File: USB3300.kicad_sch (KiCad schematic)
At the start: 48 parts, among them J1 SWD, J3 USB_C_Receptacle_USB2.0_14P, SW1 SW_SPDT, U1 USB3300-EZK, U2 STM32F405RGT6, U3 XC6206PxxxMR, U4 SRV05-4, Y1 16MHz, Y2 24MHz

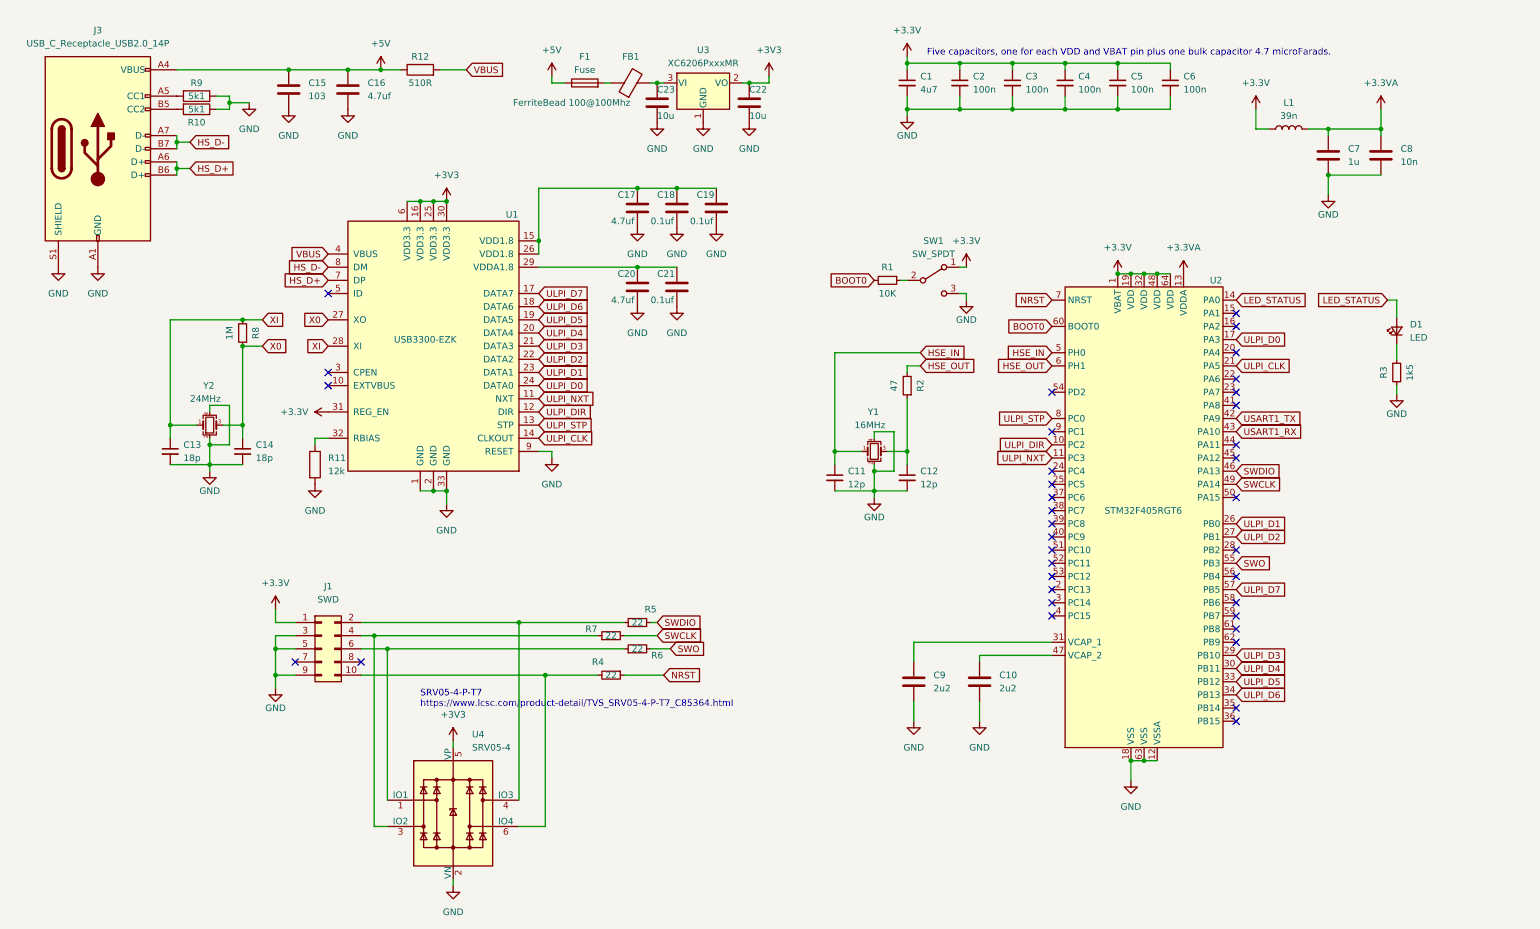
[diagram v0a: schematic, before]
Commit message: Added power_flags to lower the amount of warnings, fixed +3V3 label
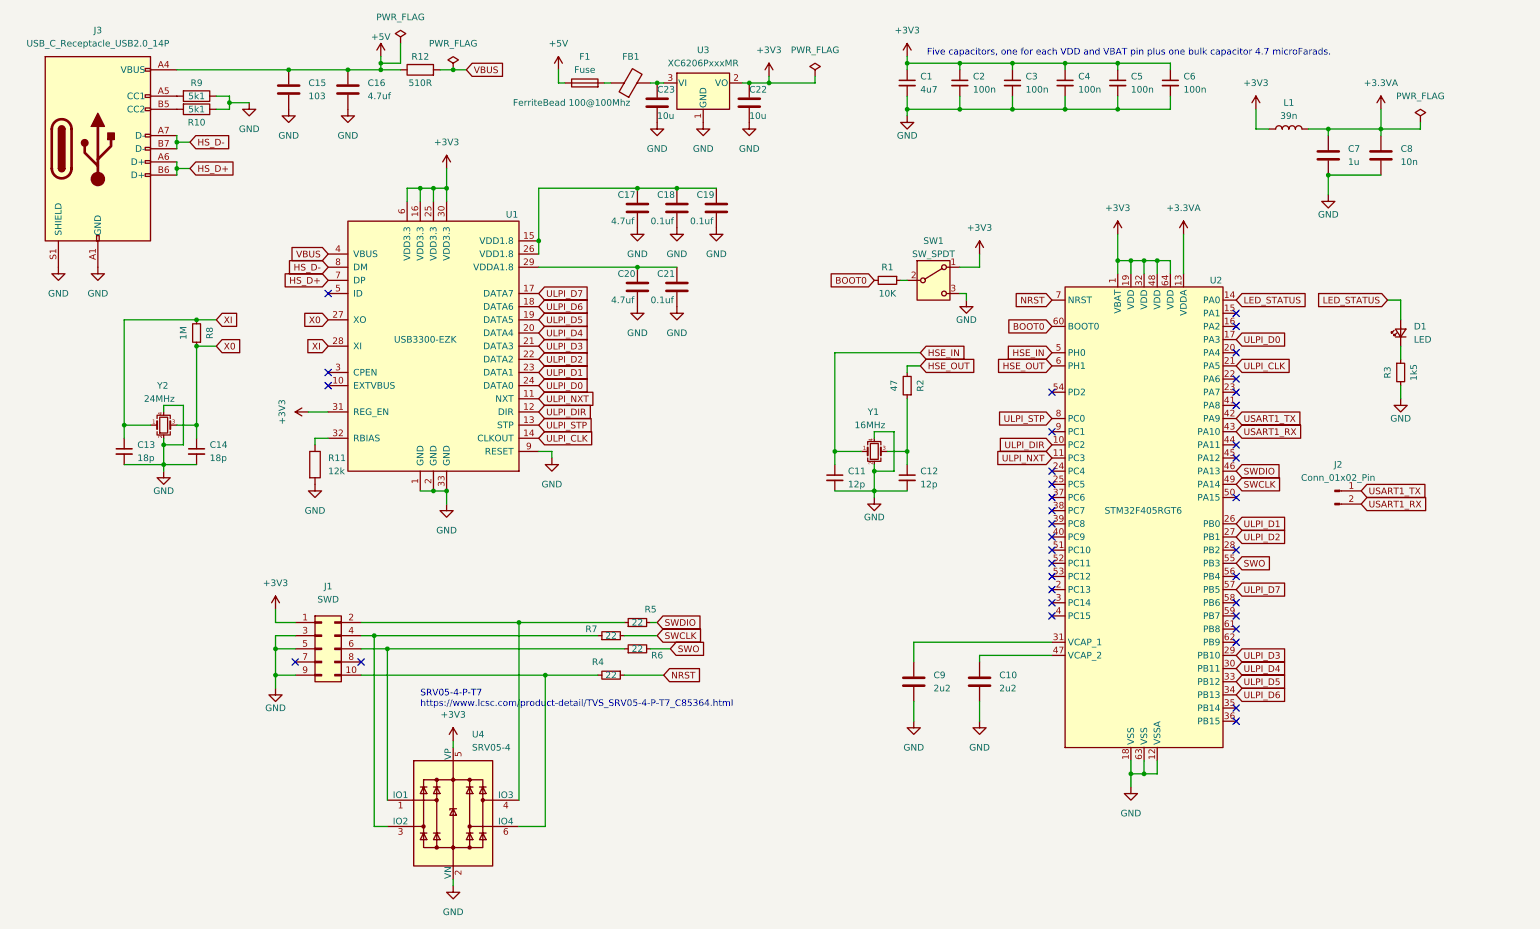
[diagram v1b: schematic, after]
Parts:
- added J2: Conn_01x02_Pin, symbol Connector:Conn_01x02_Pin
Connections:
- net +3.3V is gone; now on net +3V3: L1.1, U1.31 (REG_EN), U2.1 (VBAT), U2.19 (VDD), U2.32 (VDD), U2.48 (VDD), U2.64 (VDD)
- net USART1_RX: now also J2.2 (Pin_2)
- net USART1_TX: now also J2.1 (Pin_1)
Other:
- moved on the sheet: C13, C14, D1, R3, R8, Y2

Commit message: layout
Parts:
- C10, C15, C16, C17, C18, C19, C20, C21, C22, C23, C7, C8, C9: footprint (none) -> Capacitor_SMD:C_0603_1608Metric
- C13, C14, C2, C3, C4, C5, C6: footprint Capacitor_SMD:C_0402_1005Metric -> Capacitor_SMD:C_0603_1608Metric
- F1: footprint (none) -> Fuse:Fuse_1206_3216Metric_Pad1.42x1.75mm_HandSolder
- FB1: footprint (none) -> Ferrite_THT:LairdTech_28C0236-0JW-10
- J2: footprint (none) -> Connector_PinHeader_2.54mm:PinHeader_1x02_P2.54mm_Vertical
- J3: footprint (none) -> Connector_USB:USB_Micro-B_Molex-105017-0001
- L1: footprint (none) -> Inductor_SMD:L_0603_1608Metric
- R10, R11, R12, R9: footprint (none) -> Resistor_SMD:R_0603_1608Metric
- R2, R4, R5, R6, R7, R8: footprint Resistor_SMD:R_0402_1005Metric -> Resistor_SMD:R_0603_1608Metric
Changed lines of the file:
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@@
       (effects (font (size 1.27 1.27)) (justify left))
     )
-    (property "Footprint" "" (at 65.7352 29.21 0)
+    (property "Footprint" "Capacitor_SMD:C_0603_1608Metric" (at 65.7352 29.21 0)
       (effects (font (size 1.27 1.27)) hide)
     )
@@
       (effects (font (size 1.27 1.27)) (justify left))
     )
-    (property "Footprint" "Capacitor_SMD:C_0402_1005Metric" (at 194.31 24.13 0)
+    (property "Footprint" "Capacitor_SMD:C_0603_1608Metric" (at 194.31 24.13 0)
       (effects (font (size 1.27 1.27)) hide)
     )
@@
       (effects (font (size 1.27 1.27)))
     )
-    (property "Footprint" "" (at 46.99 27.432 90)
+    (property "Footprint" "Resistor_SMD:R_0603_1608Metric" (at 46.99 27.432 90)
       (effects (font (size 1.27 1.27)) hide)
     )
@@
       (effects (font (size 1.27 1.27)))
     )
-    (property "Footprint" "Resistor_SMD:R_0402_1005Metric" (at 132.08 128.27 0)
+    (property "Footprint" "Resistor_SMD:R_0603_1608Metric" (at 132.08 128.27 0)
       (effects (font (size 1.27 1.27)) hide)
     )
@@
       (effects (font (size 1.27 1.27)))
     )
-    (property "Footprint" "Resistor_SMD:R_0402_1005Metric" (at 184.15 82.55 0)
+    (property "Footprint" "Resistor_SMD:R_0603_1608Metric" (at 184.15 82.55 0)
       (effects (font (size 1.27 1.27)) hide)
     )
@@
       (effects (font (size 1.27 1.27)) (justify left))
     )
-    (property "Footprint" "Capacitor_SMD:C_0402_1005Metric" (at 224.79 24.13 0)
+    (property "Footprint" "Capacitor_SMD:C_0603_1608Metric" (at 224.79 24.13 0)
       (effects (font (size 1.27 1.27)) hide)
     )
@@
       (effects (font (size 1.27 1.27)) (justify left))
     )
-    (property "Footprint" "Capacitor_SMD:C_0402_1005Metric" (at 234.95 24.13 0)
+    (property "Footprint" "Capacitor_SMD:C_0603_1608Metric" (at 234.95 24.13 0)
       (effects (font (size 1.27 1.27)) hide)
     )
@@
       (effects (font (size 1.27 1.27)))
     )
-    (property "Footprint" "" (at 121.92 25.908 90)
+    (property "Footprint" "Fuse:Fuse_1206_3216Metric_Pad1.42x1.75mm_HandSolder" (at 121.92 25.908 90)
       (effects (font (size 1.27 1.27)) hide)
     )
@@
       (effects (font (size 1.27 1.27)) (justify left))
     )
-    (property "Footprint" "" (at 276.5552 41.91 0)
+    (property "Footprint" "Capacitor_SMD:C_0603_1608Metric" (at 276.5552 41.91 0)
       (effects (font (size 1.27 1.27)) hide)
     )
@@
       (effects (font (size 1.27 1.27)) (justify left))
     )
-    (property "Footprint" "" (at 77.1652 29.21 0)
+    (property "Footprint" "Capacitor_SMD:C_0603_1608Metric" (at 77.1652 29.21 0)
       (effects (font (size 1.27 1.27)) hide)
     )
@@
       (effects (font (size 1.27 1.27)))
     )
-    (property "Footprint" "" (at 31.75 36.83 0)
+    (property "Footprint" "Connector_USB:USB_Micro-B_Molex-105017-0001" (at 31.75 36.83 0)
       (effects (font (size 1.27 1.27)) hide)
     )
@@
       (effects (font (size 1.27 1.27)))
     )
-    (property "Footprint" "Resistor_SMD:R_0402_1005Metric" (at 127 138.43 0)
+    (property "Footprint" "Resistor_SMD:R_0603_1608Metric" (at 127 138.43 0)
       (effects (font (size 1.27 1.27)) hide)
     )
@@
       (effects (font (size 1.27 1.27)) (justify left))
     )
-    (property "Footprint" "" (at 186.3852 143.51 0)
+    (property "Footprint" "Capacitor_SMD:C_0603_1608Metric" (at 186.3852 143.51 0)
       (effects (font (size 1.27 1.27)) hide)
     )
@@
       (effects (font (size 1.27 1.27)))
     )
-    (property "Footprint" "" (at 130.81 25.908 90)
+    (property "Footprint" "Ferrite_THT:LairdTech_28C0236-0JW-10" (at 130.81 25.908 90)
       (effects (font (size 1.27 1.27)) hide)
     )
@@
       (effects (font (size 1.27 1.27)))
     )
-    (property "Footprint" "" (at 257.81 33.02 0)
+    (property "Footprint" "Inductor_SMD:L_0603_1608Metric" (at 257.81 33.02 0)
       (effects (font (size 1.27 1.27)) hide)
     )
@@
       (effects (font (size 1.27 1.27)))
     )
-    (property "Footprint" "" (at 46.99 24.892 90)
+    (property "Footprint" "Resistor_SMD:R_0603_1608Metric" (at 46.99 24.892 90)
       (effects (font (size 1.27 1.27)) hide)
     )
@@
       (effects (font (size 1.27 1.27)) (justify left))
     )
-    (property "Footprint" "Capacitor_SMD:C_0402_1005Metric" (at 46.99 95.25 0)
+    (property "Footprint" "Capacitor_SMD:C_0603_1608Metric" (at 46.99 95.25 0)
       (effects (font (size 1.27 1.27)) hide)
     )
@@
       (effects (font (size 1.27 1.27)) (justify left))
     )
-    (property "Footprint" "" (at 154.6352 31.75 0)
+    (property "Footprint" "Capacitor_SMD:C_0603_1608Metric" (at 154.6352 31.75 0)
       (effects (font (size 1.27 1.27)) hide)
     )
@@
       (effects (font (size 1.27 1.27)) (justify left))
     )
-    (property "Footprint" "" (at 133.0452 52.07 0)
+    (property "Footprint" "Capacitor_SMD:C_0603_1608Metric" (at 133.0452 52.07 0)
       (effects (font (size 1.27 1.27)) hide)
     )
@@
       (effects (font (size 1.27 1.27)))
     )
-    (property "Footprint" "Resistor_SMD:R_0402_1005Metric" (at 127 130.81 0)
+    (property "Footprint" "Resistor_SMD:R_0603_1608Metric" (at 127 130.81 0)
       (effects (font (size 1.27 1.27)) hide)
     )
@@
       (effects (font (size 1.27 1.27)) (justify left))
     )
-    (property "Footprint" "" (at 148.2852 52.07 0)
+    (property "Footprint" "Capacitor_SMD:C_0603_1608Metric" (at 148.2852 52.07 0)
       (effects (font (size 1.27 1.27)) hide)
     )
@@
       (effects (font (size 1.27 1.27)))
     )
-    (property "Footprint" "Resistor_SMD:R_0402_1005Metric" (at 132.08 133.35 0)
+    (property "Footprint" "Resistor_SMD:R_0603_1608Metric" (at 132.08 133.35 0)
       (effects (font (size 1.27 1.27)) hide)
     )
@@
       (effects (font (size 1.27 1.27)) (justify left))
     )
-    (property "Footprint" "" (at 266.3952 41.91 0)
+    (property "Footprint" "Capacitor_SMD:C_0603_1608Metric" (at 266.3952 41.91 0)
       (effects (font (size 1.27 1.27)) hide)
     )
@@
       (effects (font (size 1.27 1.27)) (justify left))
     )
-    (property "Footprint" "Capacitor_SMD:C_0402_1005Metric" (at 204.47 24.13 0)
+    (property "Footprint" "Capacitor_SMD:C_0603_1608Metric" (at 204.47 24.13 0)
       (effects (font (size 1.27 1.27)) hide)
     )
@@
       (effects (font (size 1.27 1.27)) (justify left))
     )
-    (property "Footprint" "" (at 136.8552 31.75 0)
+    (property "Footprint" "Capacitor_SMD:C_0603_1608Metric" (at 136.8552 31.75 0)
       (effects (font (size 1.27 1.27)) hide)
     )
@@
       (effects (font (size 1.27 1.27)) (justify left))
     )
-    (property "Footprint" "" (at 133.0452 67.31 0)
+    (property "Footprint" "Capacitor_SMD:C_0603_1608Metric" (at 133.0452 67.31 0)
       (effects (font (size 1.27 1.27)) hide)
     )
@@
       (effects (font (size 1.27 1.27)) (justify left))
     )
-    (property "Footprint" "" (at 199.0852 143.51 0)
+    (property "Footprint" "Capacitor_SMD:C_0603_1608Metric" (at 199.0852 143.51 0)
       (effects (font (size 1.27 1.27)) hide)
     )
@@
       (effects (font (size 1.27 1.27)))
     )
-    (property "Footprint" "" (at 90.17 23.368 90)
+    (property "Footprint" "Resistor_SMD:R_0603_1608Metric" (at 90.17 23.368 90)
       (effects (font (size 1.27 1.27)) hide)
     )
@@
       (effects (font (size 1.27 1.27)) (justify left))
     )
-    (property "Footprint" "" (at 140.6652 52.07 0)
+    (property "Footprint" "Capacitor_SMD:C_0603_1608Metric" (at 140.6652 52.07 0)
       (effects (font (size 1.27 1.27)) hide)
     )
@@
       (effects (font (size 1.27 1.27)) (justify left))
     )
-    (property "Footprint" "Capacitor_SMD:C_0402_1005Metric" (at 214.63 24.13 0)
+    (property "Footprint" "Capacitor_SMD:C_0603_1608Metric" (at 214.63 24.13 0)
       (effects (font (size 1.27 1.27)) hide)
     )
@@
       (effects (font (size 1.27 1.27)))
     )
-    (property "Footprint" "Resistor_SMD:R_0402_1005Metric" (at 46.99 72.39 0)
+    (property "Footprint" "Resistor_SMD:R_0603_1608Metric" (at 46.99 72.39 0)
       (effects (font (size 1.27 1.27)) hide)
     )
@@
       (effects (font (size 1.27 1.27)) (justify left))
     )
-    (property "Footprint" "Capacitor_SMD:C_0402_1005Metric" (at 33.02 95.25 0)
+    (property "Footprint" "Capacitor_SMD:C_0603_1608Metric" (at 33.02 95.25 0)
       (effects (font (size 1.27 1.27)) hide)
     )
@@
       (effects (font (size 1.27 1.27)))
     )
-    (property "Footprint" "" (at 266.7 102.87 0)
+    (property "Footprint" "Connector_PinHeader_2.54mm:PinHeader_1x02_P2.54mm_Vertical" (at 266.7 102.87 0)
       (effects (font (size 1.27 1.27)) hide)
     )
@@
       (effects (font (size 1.27 1.27)) (justify left))
     )
-    (property "Footprint" "" (at 140.6652 67.31 0)
+    (property "Footprint" "Capacitor_SMD:C_0603_1608Metric" (at 140.6652 67.31 0)
       (effects (font (size 1.27 1.27)) hide)
     )
@@
       (effects (font (size 1.27 1.27)) (justify left))
     )
-    (property "Footprint" "" (at 68.072 97.79 90)
-      (effects (font (size 1.27 1.27)) hide)
-    )
+    (property "Footprint" "Resistor_SMD:R_0603_1608Metric" (at 68.072 97.79 90)
+      (effects (font (size 1.27 1.27)) hide)
+    )

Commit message: work on pcb
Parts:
- added C24: 100n, symbol Device:C
- J3: footprint Connector_USB:USB_Micro-B_Molex-105017-0001 -> Connector_USB:USB_C_Receptacle_HRO_TYPE-C-31-M-12
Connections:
- net GND: now also C24.2
- net NRST: now also C24.1
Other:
- note added: "pull up"
- note added: "pull up 10k am uart auf 3V3"
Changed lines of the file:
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@@
   (junction (at 64.77 21.59) (diameter 0) (color 0 0 0 0)
+  )
+  (junction (at 134.62 138.43) (diameter 0) (color 0 0 0 0)
   )
   (junction (at 132.08 59.69) (diameter 0) (color 0 0 0 0)
@@
     (stroke (width 0) (type default))
   )
-  (wire (pts (xy 129.54 138.43) (xy 137.16 138.43))
+  (wire (pts (xy 129.54 138.43) (xy 134.62 138.43))
     (stroke (width 0) (type default))
   )
@@
     (stroke (width 0) (type default))
   )
+  (wire (pts (xy 134.62 138.43) (xy 134.62 151.13))
+    (stroke (width 0) (type default))
+  )
   (wire (pts (xy 184.15 85.09) (xy 184.15 95.25))
     (stroke (width 0) (type solid))
@@
     (stroke (width 0) (type default))
   )
+  (wire (pts (xy 134.62 138.43) (xy 137.16 138.43))
+    (stroke (width 0) (type default))
+  )
   (wire (pts (xy 214.63 29.21) (xy 204.47 29.21))
     (stroke (width 0) (type solid))
@@
   (wire (pts (xy 251.46 29.21) (xy 251.46 33.02))
     (stroke (width 0) (type default))
+  )
+  (text "pull up" (at 59.69 91.44 0)
+    (effects (font (size 1.27 1.27)) (justify left bottom))
   )
   (text "Five capacitors, one for each VDD and VBAT pin plus one bulk capacitor 4.7 microFarads."
     (at 187.96 19.05 0)
+    (effects (font (size 1.27 1.27)) (justify left bottom))
+  )
+  (text "pull up 10k am uart auf 3V3" (at 270.51 110.49 0)
     (effects (font (size 1.27 1.27)) (justify left bottom))
   )
@@
     )
   )
+  (symbol (lib_id "Device:C") (at 134.62 154.94 0) (unit 1)
+    (in_bom yes) (on_board yes) (dnp no) (fields_autoplaced)
+    (property "Reference" "C24" (at 138.43 153.67 0)
+      (effects (font (size 1.27 1.27)) (justify left))
+    )
+    (property "Value" "100n" (at 138.43 156.21 0)
+      (effects (font (size 1.27 1.27)) (justify left))
+    )
+    (property "Footprint" "" (at 135.5852 158.75 0)
+      (effects (font (size 1.27 1.27)) hide)
+    )
+    (property "Datasheet" "~" (at 134.62 154.94 0)
+      (effects (font (size 1.27 1.27)) hide)
+    )
+    (pin "1")
+    (pin "2")
+    (instances
+      (project "USB3300"
+        (path "/09e9d231-c510-4f8a-ac7d-12061987ad81"
+          (reference "C24") (unit 1)
+        )
+      )
+    )
+  )
   (symbol (lib_id "power:GND") (at 62.23 140.97 0) (unit 1)
     (in_bom yes) (on_board yes) (dnp no)
@@
       (effects (font (size 1.27 1.27)))
     )
-    (property "Footprint" "Connector_USB:USB_Micro-B_Molex-105017-0001" (at 31.75 36.83 0)
+    (property "Footprint" "Connector_USB:USB_C_Receptacle_HRO_TYPE-C-31-M-12" (at 31.75 36.83 0)
       (effects (font (size 1.27 1.27)) hide)
     )
@@
         )
       )
+    )
+  )
+  (symbol (lib_id "power:GND") (at 134.62 158.75 0) (unit 1)
+    (in_bom yes) (on_board yes) (dnp no) (fields_autoplaced)
+    (property "Reference" "#PWR024" (at 134.62 165.1 0)
+      (effects (font (size 1.27 1.27)) hide)
+    )
+    (property "Value" "GND" (at 134.62 163.83 0)
+      (effects (font (size 1.27 1.27)))
+    )
+    (property "Footprint" "" (at 134.62 158.75 0)
+      (effects (font (size 1.27 1.27)) hide)
+    )
+    (property "Datasheet" "" (at 134.62 158.75 0)
+      (effects (font (size 1.27 1.27)) hide)
+    )
+    (pin "1")
+    (instances
+      (project "USB3300"
+        (path "/09e9d231-c510-4f8a-ac7d-12061987ad81"
+          (reference "#PWR024") (unit 1)
+        )
+      )
